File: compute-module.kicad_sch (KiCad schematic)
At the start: 100 parts, among them J201 DF40HC(3.0)-100DS-0.4v, J202 DF40HC(3.0)-100DS-0.4v, M201 compute-module-4-1.5mm, Q201 PJE138K, Q202 SSM3J332R, Q203 SSM3J332R, Q204 SSM3J332R, Q205 SSM3J332R, Q206 PJE138K, Q207 PJE138K, Q208 PJE138K, Q209 PJE138K, Q210 PJE138K, Q211 PJE138K, Q212 SSM3J332R, Q213 PJE138K, U201 TXB0104_UQFN, U203 TXB0104_UQFN, U204 MCP23017T-E_QFN

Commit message: [#53901] Update symbols & footprints from lib
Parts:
- D201, D202, D205, D206, D207: footprint antmicro-footprints:LED_0603_1608Metric_R -> antmicro-footprints:LED_0603_1608Metric_G; symbol antmicroLEDIndicationDiscrete:LED_R_0603_598-8D80-107F -> antmicroLEDIndicationDiscrete:LED_G_0603_598-8D80-107F
- J201, J202: value DF40HC(3.0)-100DS-0.4v -> Socket_Hirose_DF40_2x50_DF40HC-3.0-100DS-0.4V
- M201: value compute-module-4-1.5mm -> Compute-Module-4_H1.5mm
- R202, R205, R206, R208, R209, R230, R232, R236, R240: DNP DNP -> (none); now in the parts list
- TP201, TP202, TP203, TP204, TP205, TP206, TP207, TP208, TP209, TP210, TP212, TP213: value TP_1mm_SMD -> TP_0.75mm_SMD
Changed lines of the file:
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@@
   (title_block
     (title "CM4 Baseboard")
-    (date "2024-03-14")
+    (date "2024-03-22")
     (rev "1.0.0")
     (company "Antmicro")

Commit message: [#56708] Add loclib
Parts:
- C201, C202, C203, C204, C206, C207, C210: footprint antmicro-footprints:C_0402_1005Metric -> cm4-baseboard-footprints:C_0402_1005Metric; symbol antmicroCapacitors0402:C_100n_0402 -> cm4-baseboard:C_100n_0402
- C209: footprint antmicro-footprints:C_0402_1005Metric -> cm4-baseboard-footprints:C_0402_1005Metric; symbol antmicroCapacitors0402:C_10u_0402 -> cm4-baseboard:C_10u_0402
- D201, D202, D205, D206, D207: footprint antmicro-footprints:LED_0603_1608Metric_G -> cm4-baseboard-footprints:LED_0603_1608Metric_G; symbol antmicroLEDIndicationDiscrete:LED_G_0603_598-8D80-107F -> cm4-baseboard:LED_G_0603_598-8D80-107F
- D203, D204: footprint antmicro-footprints:XDFN-2_1x0.60mm -> cm4-baseboard-footprints:XDFN-2_1x0.60mm; symbol antmicroTVSDiodes:TPD1E0B04_XDFN-2 -> cm4-baseboard:TPD1E0B04_XDFN-2
- H201, H202, H203, H204: footprint antmicro-footprints:Spacer_Drill3.7mm_H3mm_9774030151R -> cm4-baseboard-footprints:Spacer_Drill3.7mm_H3mm_9774030151R; symbol antmicroMechanicalParts:Spacer_Drill3.7mm_H3mm_9774030151R -> cm4-baseboard:Spacer_Drill3.7mm_H3mm_9774030151R
- J201, J202: footprint antmicro-footprints:Conn_Socket_Hirose_DF40_2x50_DF40HC-3.0-100DS-0.4V -> cm4-baseboard-footprints:Conn_Socket_Hirose_DF40_2x50_DF40HC-3.0-100DS-0.4V; symbol antmicroB2BConnectors:Socket_Hirose_DF40_2x50_DF40HC-3.0-100DS-0.4V -> cm4-baseboard:Socket_Hirose_DF40_2x50_DF40HC-3.0-100DS-0.4V
- M201: footprint antmicro-footprints:Compute-Module-4_H1.5mm -> cm4-baseboard-footprints:Compute-Module-4_H1.5mm; symbol antmicroModules:Compute-Module-4_H1.5mm -> cm4-baseboard:Compute-Module-4_H1.5mm
- Q201, Q206, Q207, Q208, Q209, Q210, Q211, Q213: footprint antmicro-footprints:SOT-523 -> cm4-baseboard-footprints:SOT-523; symbol antmicroTransistorsFETsMOSFETsSingle:PJE138K -> cm4-baseboard:PJE138K
- Q202, Q203, Q204, Q205, Q212: footprint antmicro-footprints:SOT-23-3 -> cm4-baseboard-footprints:SOT-23-3; symbol antmicroTransistorsFETsMOSFETsSingle:SSM3J332R -> cm4-baseboard:SSM3J332R
- R201, R202, R205, R206, R208, R209, R216, R217, R218, R219, R220, R221, R222, R223, R225, R226, R227, R228, R239, R240, R258, R259: footprint antmicro-footprints:R_0402_1005Metric -> cm4-baseboard-footprints:R_0402_1005Metric; symbol antmicroResistors0402:R_0R_0402 -> cm4-baseboard:R_0R_0402
- R203, R204, R214, R260, R261: footprint antmicro-footprints:R_0402_1005Metric -> cm4-baseboard-footprints:R_0402_1005Metric; symbol antmicroResistors0402:R_100k_0402 -> cm4-baseboard:R_100k_0402
- R207, R210, R215, R224: footprint antmicro-footprints:R_0402_1005Metric -> cm4-baseboard-footprints:R_0402_1005Metric; symbol antmicroResistors0402:R_1k_0402 -> cm4-baseboard:R_1k_0402
- R211: footprint antmicro-footprints:R_0402_1005Metric -> cm4-baseboard-footprints:R_0402_1005Metric; symbol antmicroResistors0402:R_470R_0402 -> cm4-baseboard:R_470R_0402
- R212, R213: footprint antmicro-footprints:R_0402_1005Metric -> cm4-baseboard-footprints:R_0402_1005Metric; symbol antmicroResistors0402:R_200k_0402 -> cm4-baseboard:R_200k_0402
- R229: footprint antmicro-footprints:R_0402_1005Metric -> cm4-baseboard-footprints:R_0402_1005Metric; symbol antmicroResistors0402:R_100R_0402 -> cm4-baseboard:R_100R_0402
- R230, R231, R232, R233, R234, R235, R236, R237, R238: footprint antmicro-footprints:R_0402_1005Metric -> cm4-baseboard-footprints:R_0402_1005Metric; symbol antmicroResistors0402:R_10k_0402 -> cm4-baseboard:R_10k_0402
- R241, R243: footprint antmicro-footprints:R_0402_1005Metric -> cm4-baseboard-footprints:R_0402_1005Metric; symbol antmicroResistors0402:R_2k2_0402 -> cm4-baseboard:R_2k2_0402
- R242: footprint antmicro-footprints:R_0402_1005Metric -> cm4-baseboard-footprints:R_0402_1005Metric; symbol antmicroResistors0402:R_200R_0402 -> cm4-baseboard:R_200R_0402
- S201, S202: footprint antmicro-footprints:SW_KMR211NGLFS_SMD -> cm4-baseboard-footprints:SW_KMR211NGLFS_SMD; symbol antmicroPushbuttonSwitches:SW_KMR211NGLFS_SMD -> cm4-baseboard:SW_KMR211NGLFS_SMD
- S203: footprint antmicro-footprints:Switch_Slide_CAS-120TA -> cm4-baseboard-footprints:Switch_Slide_CAS-120TA; symbol antmicroSlideSwitches:CAS-120TA -> cm4-baseboard:CAS-120TA
- TP201, TP202, TP203, TP204, TP205, TP206, TP207, TP208, TP209, TP210, TP212, TP213: footprint antmicro-footprints:TP_SMD_0.75mm -> cm4-baseboard-footprints:TP_SMD_0.75mm; symbol antmicroTestPoints:TP_0.75mm_SMD -> cm4-baseboard:TP_0.75mm_SMD
- U201, U203: footprint antmicro-footprints:UQFN-12_2x1.7mm_P0.4mm_Texas_RUT -> cm4-baseboard-footprints:UQFN-12_2x1.7mm_P0.4mm_Texas_RUT; symbol antmicroLogicTranslatorsLevelShifters:TXB0104_UQFN -> cm4-baseboard:TXB0104_UQFN
- U204: footprint antmicro-footprints:QFN-28-1EP_6x6mm_P0.65mm_EP3.7x3.7mm -> cm4-baseboard-footprints:QFN-28-1EP_6x6mm_P0.65mm_EP3.7x3.7mm; symbol antmicroInterfaceIOExpanders:MCP23017T-E_QFN -> cm4-baseboard:MCP23017T-E_QFN

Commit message: [#56708] Update symbol/footprint props; Update modules visibilty
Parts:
- D201, D202, D205, D206, D207: value LED_G -> LED_G_0603_598-8D80-107F; Color (none) -> Green
- R202, R205, R206, R208, R209, R230, R232, R236, R240: DNP (none) -> DNP; now left out of the parts list

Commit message: [#57456] Remove loclib
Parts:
- C201, C202, C203, C204, C206, C207, C210: footprint cm4-baseboard-footprints:C_0402_1005Metric -> antmicro-footprints:C_0402_1005Metric; symbol cm4-baseboard:C_100n_0402 -> antmicroCapacitors0402:C_100n_0402
- C209: footprint cm4-baseboard-footprints:C_0402_1005Metric -> antmicro-footprints:C_0402_1005Metric; symbol cm4-baseboard:C_10u_0402 -> antmicroCapacitors0402:C_10u_0402
- D201, D202, D205, D206, D207: footprint cm4-baseboard-footprints:LED_0603_1608Metric_G -> antmicro-footprints:LED_0603_1608Metric_G; symbol cm4-baseboard:LED_G_0603_598-8D80-107F -> antmicroLEDIndicationDiscrete:LED_G_0603_598-8D80-107F
- D203, D204: footprint cm4-baseboard-footprints:XDFN-2_1x0.60mm -> antmicro-footprints:XDFN-2_1x0.60mm; symbol cm4-baseboard:TPD1E0B04_XDFN-2 -> antmicroTVSDiodes:TPD1E0B04_XDFN-2
- H201, H202, H203, H204: footprint cm4-baseboard-footprints:Spacer_Drill3.7mm_H3mm_9774030151R -> antmicro-footprints:Spacer_Drill3.7mm_H3mm_9774030151R; symbol cm4-baseboard:Spacer_Drill3.7mm_H3mm_9774030151R -> antmicroMechanicalParts:Spacer_Drill3.7mm_H3mm_9774030151R
- J201, J202: footprint cm4-baseboard-footprints:Conn_Socket_Hirose_DF40_2x50_DF40HC-3.0-100DS-0.4V -> antmicro-footprints:Conn_Socket_Hirose_DF40_2x50_DF40HC-3.0-100DS-0.4V; symbol cm4-baseboard:Socket_Hirose_DF40_2x50_DF40HC-3.0-100DS-0.4V -> antmicroB2BConnectors:Socket_Hirose_DF40_2x50_DF40HC-3.0-100DS-0.4V
- M201: footprint cm4-baseboard-footprints:Compute-Module-4_H1.5mm -> antmicro-footprints:Compute-Module-4_H1.5mm; symbol cm4-baseboard:Compute-Module-4_H1.5mm -> antmicroModules:Compute-Module-4_H1.5mm
- Q201, Q206, Q207, Q208, Q209, Q210, Q211, Q213: footprint cm4-baseboard-footprints:SOT-523 -> antmicro-footprints:SOT-523; symbol cm4-baseboard:PJE138K -> antmicroTransistorsFETsMOSFETsSingle:PJE138K
- Q202, Q203, Q204, Q205, Q212: footprint cm4-baseboard-footprints:SOT-23-3 -> antmicro-footprints:SOT-23-3; symbol cm4-baseboard:SSM3J332R -> antmicroTransistorsFETsMOSFETsSingle:SSM3J332R
- R201, R202, R205, R206, R208, R209, R216, R217, R218, R219, R220, R221, R222, R223, R225, R226, R227, R228, R239, R240, R258, R259: footprint cm4-baseboard-footprints:R_0402_1005Metric -> antmicro-footprints:R_0402_1005Metric; symbol cm4-baseboard:R_0R_0402 -> antmicroResistors0402:R_0R_0402
- R203, R204, R214, R260, R261: footprint cm4-baseboard-footprints:R_0402_1005Metric -> antmicro-footprints:R_0402_1005Metric; symbol cm4-baseboard:R_100k_0402 -> antmicroResistors0402:R_100k_0402
- R207, R210, R215, R224: footprint cm4-baseboard-footprints:R_0402_1005Metric -> antmicro-footprints:R_0402_1005Metric; symbol cm4-baseboard:R_1k_0402 -> antmicroResistors0402:R_1k_0402
- R211: footprint cm4-baseboard-footprints:R_0402_1005Metric -> antmicro-footprints:R_0402_1005Metric; symbol cm4-baseboard:R_470R_0402 -> antmicroResistors0402:R_470R_0402
- R212, R213: footprint cm4-baseboard-footprints:R_0402_1005Metric -> antmicro-footprints:R_0402_1005Metric; symbol cm4-baseboard:R_200k_0402 -> antmicroResistors0402:R_200k_0402
- R229: footprint cm4-baseboard-footprints:R_0402_1005Metric -> antmicro-footprints:R_0402_1005Metric; symbol cm4-baseboard:R_100R_0402 -> antmicroResistors0402:R_100R_0402
- R230, R231, R232, R233, R234, R235, R236, R237, R238: footprint cm4-baseboard-footprints:R_0402_1005Metric -> antmicro-footprints:R_0402_1005Metric; symbol cm4-baseboard:R_10k_0402 -> antmicroResistors0402:R_10k_0402
- R241, R243: footprint cm4-baseboard-footprints:R_0402_1005Metric -> antmicro-footprints:R_0402_1005Metric; symbol cm4-baseboard:R_2k2_0402 -> antmicroResistors0402:R_2k2_0402
- R242: footprint cm4-baseboard-footprints:R_0402_1005Metric -> antmicro-footprints:R_0402_1005Metric; symbol cm4-baseboard:R_200R_0402 -> antmicroResistors0402:R_200R_0402
- S201, S202: footprint cm4-baseboard-footprints:SW_KMR211NGLFS_SMD -> antmicro-footprints:SW_KMR211NGLFS_SMD; symbol cm4-baseboard:SW_KMR211NGLFS_SMD -> antmicroPushbuttonSwitches:SW_KMR211NGLFS_SMD
- S203: footprint cm4-baseboard-footprints:Switch_Slide_CAS-120TA -> antmicro-footprints:Switch_Slide_CAS-120TA; symbol cm4-baseboard:CAS-120TA -> antmicroSlideSwitches:CAS-120TA
- TP201, TP202, TP203, TP204, TP205, TP206, TP207, TP208, TP209, TP210, TP212, TP213: footprint cm4-baseboard-footprints:TP_SMD_0.75mm -> antmicro-footprints:TP_SMD_0.75mm; symbol cm4-baseboard:TP_0.75mm_SMD -> antmicroTestPoints:TP_0.75mm_SMD
- U201, U203: footprint cm4-baseboard-footprints:UQFN-12_2x1.7mm_P0.4mm_Texas_RUT -> antmicro-footprints:UQFN-12_2x1.7mm_P0.4mm_Texas_RUT; symbol cm4-baseboard:TXB0104_UQFN -> antmicroLogicTranslatorsLevelShifters:TXB0104_UQFN
- U204: footprint cm4-baseboard-footprints:QFN-28-1EP_6x6mm_P0.65mm_EP3.7x3.7mm -> antmicro-footprints:QFN-28-1EP_6x6mm_P0.65mm_EP3.7x3.7mm; symbol cm4-baseboard:MCP23017T-E_QFN -> antmicroInterfaceIOExpanders:MCP23017T-E_QFN
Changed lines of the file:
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@@
   (title_block
     (title "CM4 Baseboard")
-    (date "2024-03-22")
-    (rev "1.0.0")
+    (date "2024-04-08")
+    (rev "1.0.1")
     (company "Antmicro")
     (comment 1 "www.antmicro.com")

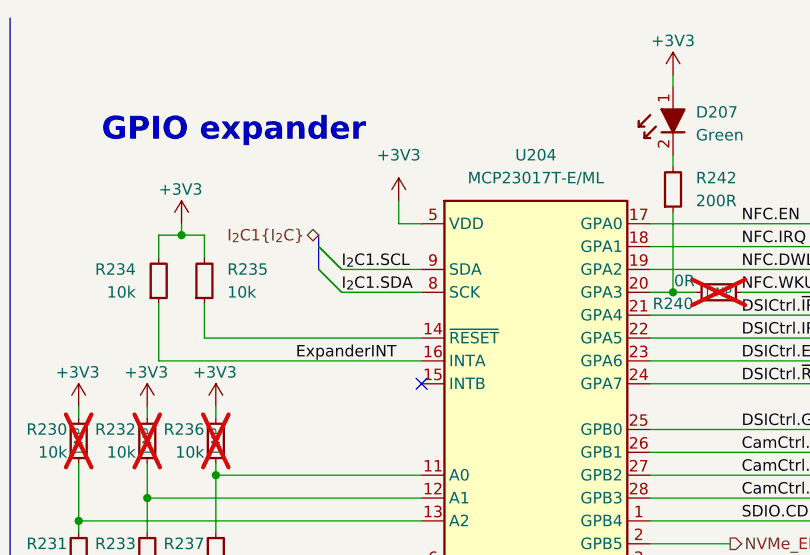
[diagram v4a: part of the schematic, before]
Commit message: [#58124] Fix GPIO expander I2C
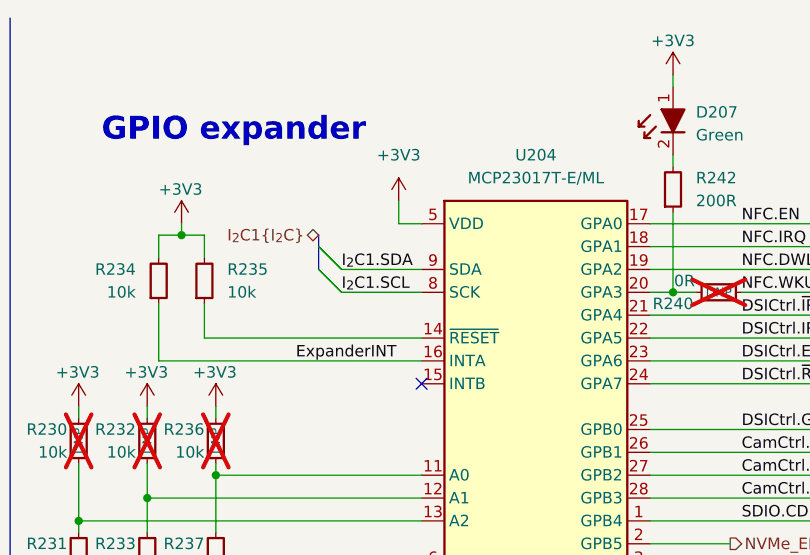
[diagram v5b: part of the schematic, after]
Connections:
- net I_{2}C1.SCL: now also U204.8 (SCK); no longer U204.9 (SDA)
- net I_{2}C1.SDA: now also U204.9 (SDA); no longer U204.8 (SCK)

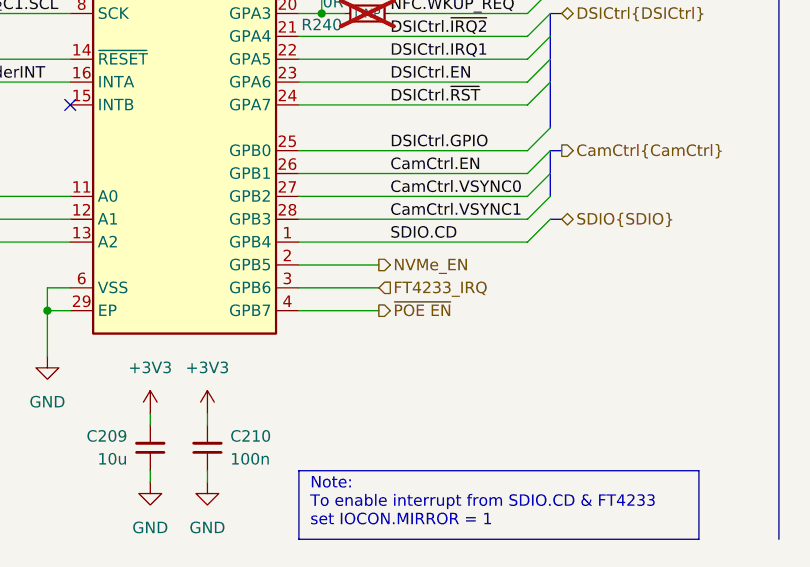
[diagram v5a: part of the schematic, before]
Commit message: [#58134] Remove I2C connection to FT4233
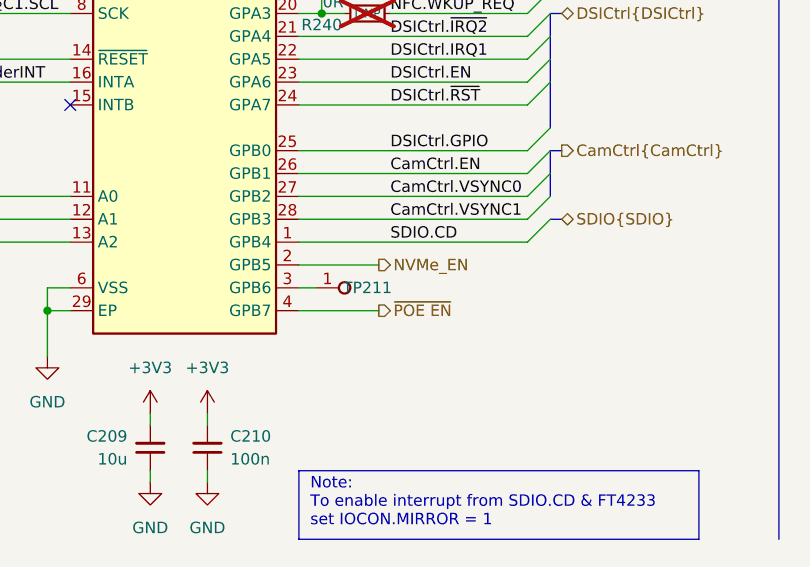
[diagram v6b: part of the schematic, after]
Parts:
- added TP211: TP_0.75mm_SMD, antmicro-footprints:TP_SMD_0.75mm, symbol antmicroTestPoints:TP_0.75mm_SMD
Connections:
- net FT4233_IRQ: no longer names the net of U204.3 (GPB6)
- net FT4233_IRQ: now also TP211.1
